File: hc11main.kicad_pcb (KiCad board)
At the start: 2 copper layers, 100 x 71 mm, 76 parts, among them J1 SPI, J2 CONN_I2C, J3 CONN_PWR, J4 CONN_LED, J5 CONN_UART, P1 CONN_2X20, T1 BS170/2N7000 (SOT23), T2 BS170/2N7000 (SOT23), U1 74LS138, U10 74LS10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

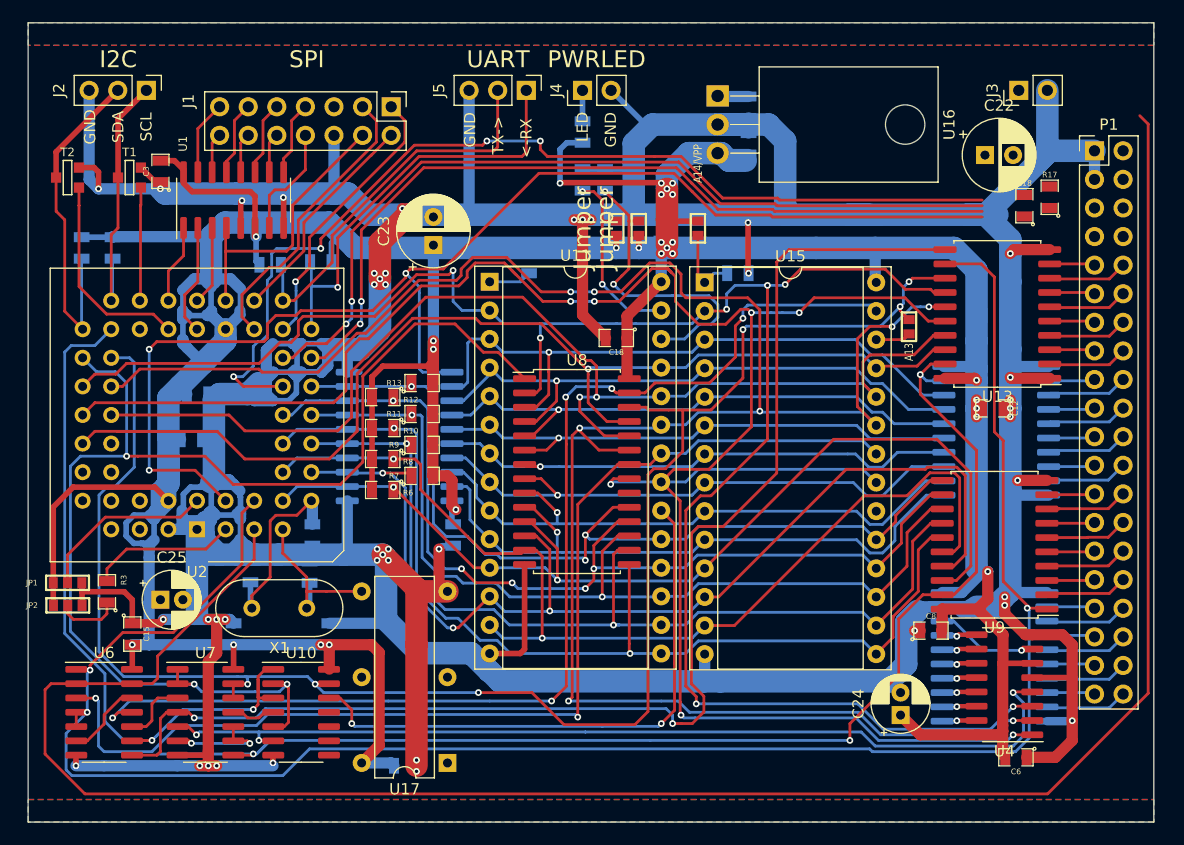
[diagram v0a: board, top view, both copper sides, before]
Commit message: finish routing everything, optimize routing, fix 2 missing CS traces
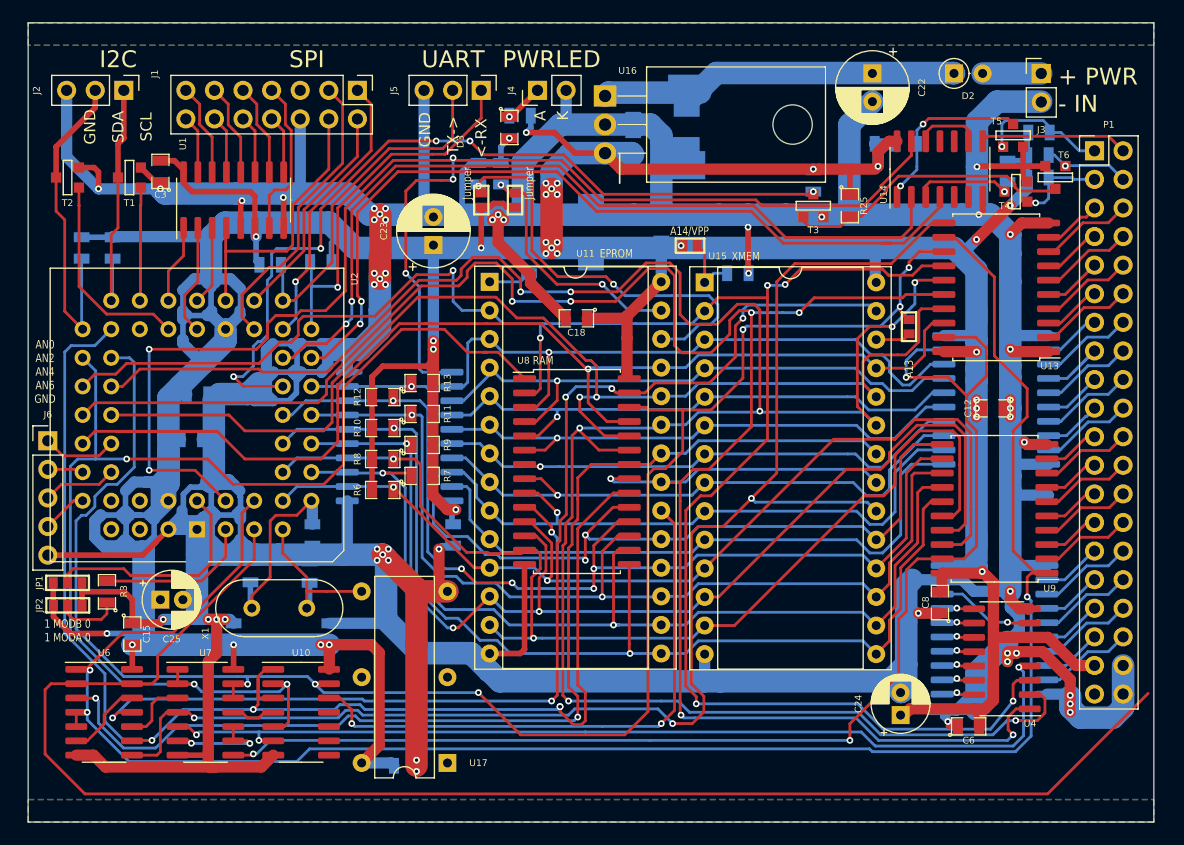
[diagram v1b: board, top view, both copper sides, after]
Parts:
- removed R17, R18: 100k, hc11:0805_m2012
- added C13: 100n, hc11:0805_m2012, B.Cu at (89.2, 25.8)
- added D1: SMBJ15A, hc11:D_SMB, B.Cu at (73.5, 24.2)
- added D2: Schottky, Diode_THT:D_DO-35_SOD27_P2.54mm_Vertical_AnodeUp, F.Cu at (97.2, 19.5)
- added D3: LED, hc11:0805_m2012, F.Cu at (57.8, 24.3)
- added D4: SMCJ15A, hc11:D_SMC, B.Cu at (73.5, 24.2)
- added D5: SMBJ5A, hc11:D_SMB, B.Cu at (65.0, 33.6)
- added J6: Conn_01x05, hc11:PinHeader_1x05_P2.54mm_Vertical, F.Cu at (16.8, 52.1)
- added R22: 10k, hc11:0805_m2012, B.Cu at (84.8, 29.0)
- added R23: 10k, hc11:0805_m2012, B.Cu at (102.0, 28.2)
- added R24: 10k, hc11:0805_m2012, B.Cu at (93.0, 25.8)
- added R25: 10k, hc11:0805_m2012, F.Cu at (88.0, 31.2)
- added R26: 10k, hc11:0805_m2012, B.Cu at (104.7, 28.8)
- added R27: 10k, hc11:0805_m2012, B.Cu at (104.8, 24.8)
- added R28: 10k, hc11:0805_m2012, B.Cu at (104.7, 26.8)
- added T3: BS170, hc11:SOT23GDS, F.Cu at (84.8, 31.2)
- added T4: BS170, hc11:SOT23GDS, F.Cu at (102.8, 30.0)
- added T5: BS170, hc11:SOT23GDS, F.Cu at (102.5, 25.0)
- added T6: BS170, hc11:SOT23GDS, F.Cu at (106.2, 28.7)
- added U14: 74HCT04, hc11:SOIC-14_3.9x8.7mm_P1.27mm, F.Cu at (96.0, 28.0)
- moved JP6 14.2 mm to (55.2, 30.8)
- moved C22 12.4 mm to (90.0, 19.5), turned to 270 degrees
- moved R15 11.3 mm to (55.0, 28.4)
- moved C19 10.3 mm to (68.8, 22.4)
- moved C20 10.2 mm to (68.8, 25.8)
- moved U16 10.0 mm to (66.2, 21.5)
- moved JP5 9.34 mm to (58.2, 30.8)
- moved R16 7.27 mm to (57.0, 28.4)
- moved R20 5.73 mm to (58.7, 23.2), turned to 180 degrees
- moved C6 5.02 mm to (98.5, 77.5), turned to 0 degrees
- moved J4 4.00 mm to (60.2, 21.0)
- moved J5 4.00 mm to (55.2, 21.0)
- moved C18 3.96 mm to (63.7, 41.2)
- moved J1 3.34 mm to (44.2, 21.0)
- moved U9 3.19 mm to (100.8, 58.2)
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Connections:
- net Net-(JP5-Pad1) renamed /EP_A14
- net Net-(JP6-Pad1) renamed /EP_A13
- J1 pad 10: /SPICS5 -> /SPICS4
- J1 pad 11: /SPICS2 -> /SPICS3
- J1 pad 12: /SPICS3 -> /SPICS2
- J1 pad 13: /SPICS0 -> /SPICS1
- J1 pad 14: /SPICS1 -> /SPICS0
- J1 pad 7: /SPICS6 -> /SPICS7
- J1 pad 8: /SPICS7 -> /SPICS6
- J1 pad 9: /SPICS4 -> /SPICS5
- P1 pad 1: GND -> /b~IRQ
- P1 pad 10: /bR~W -> /bA10
- P1 pad 11: /bA13 -> /bA9
- P1 pad 12: /bA12 -> /bA8
- P1 pad 13: /bA11 -> /bA7
- P1 pad 14: /bA10 -> /bA6
- P1 pad 15: /bA9 -> /bA5
- P1 pad 16: /bA8 -> /bA4
- P1 pad 17: /bA7 -> /bA3
- P1 pad 18: /bA6 -> /bA2
- P1 pad 19: /bA5 -> /bA1
- P1 pad 2: /bE -> /bAS
- P1 pad 20: /bA4 -> /bA0
- P1 pad 21: /bA3 -> /bD7
- P1 pad 22: /bA2 -> /bD6
- P1 pad 23: /bA1 -> /bD5
- P1 pad 24: /bA0 -> /bD4
- P1 pad 25: /bD7 -> /bD3
- P1 pad 26: /bD6 -> /bD2
- P1 pad 27: /bD5 -> /bD1
- P1 pad 28: /bD4 -> /bD0
- P1 pad 29: /bD3 -> /bS7
- P1 pad 3: GND -> /b~XIRQ
- P1 pad 30: /bD2 -> /bS6
- P1 pad 31: /bD1 -> /bS5
- P1 pad 32: /bD0 -> /bS4
- P1 pad 33: /bS7 -> /bS3
- P1 pad 34: /bS6 -> /bS2
- P1 pad 35: /bS5 -> /bS1
- P1 pad 36: /bS4 -> /bS0
- P1 pad 37: /bS3 -> VCC
- P1 pad 38: /bS2 -> GND
- P1 pad 39: /bS1 -> /bE
- P1 pad 4: VCC -> /b~RST
- P1 pad 40: /bS0 -> GND
- P1 pad 5: /bXIRQ -> /b~CSXRAM
- P1 pad 6: VCC -> /bR~W
- P1 pad 7: /bIRQ -> /bA13
- P1 pad 8: /bRST -> /bA12
- P1 pad 9: /b~CSXRAM -> /bA11
- U15 pad 20: /CSXRAM -> /~CSXRAM
- U8 pad 20: /~CSRAM -> /A15
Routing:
- net VCC: track 437.5 -> 519.5 mm, vias 26 -> 31
- net GND: track 632.6 -> 695.1 mm, vias 46 -> 50
- net /A15: track 64.8 -> 119.0 mm, vias 2 -> 4
- net /E: track 187.7 -> 136.1 mm
- net /VIN: track 2.77 -> 34.7 mm
- net /CPURST: track 0.00 -> 25.5 mm
- net /AS: track 113.8 -> 129.2 mm, vias 3 -> 5
- net /IRQ: track 0.00 -> 14.9 mm, vias 0 -> 2
- net /~CPURST: track 88.1 -> 74.1 mm, vias 4 -> 5
- net /bAS: track 0.00 -> 13.2 mm
- net /b~IRQ: track 0.00 -> 11.9 mm, vias 0 -> 1
- net /~CSXRAM: track 116.3 -> 127.6 mm, vias 2 -> 3
- net /EP_A13: track 27.6 -> 38.2 mm
- net /A11: track 194.9 -> 204.7 mm
- net /XIRQ: track 0.00 -> 9.45 mm, vias 0 -> 1
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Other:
- board text added: "+ PWR - IN"
- board text added: "1 MODB 0 1 MODA 0"
- board text added: "A"
- board text added: "AN0 AN2 AN4 AN6 GND"
- board text added: "EPROM"
- board text added: "K"
- board text added: "RAM"
- board text added: "XMEM"
- board text removed: "LED"

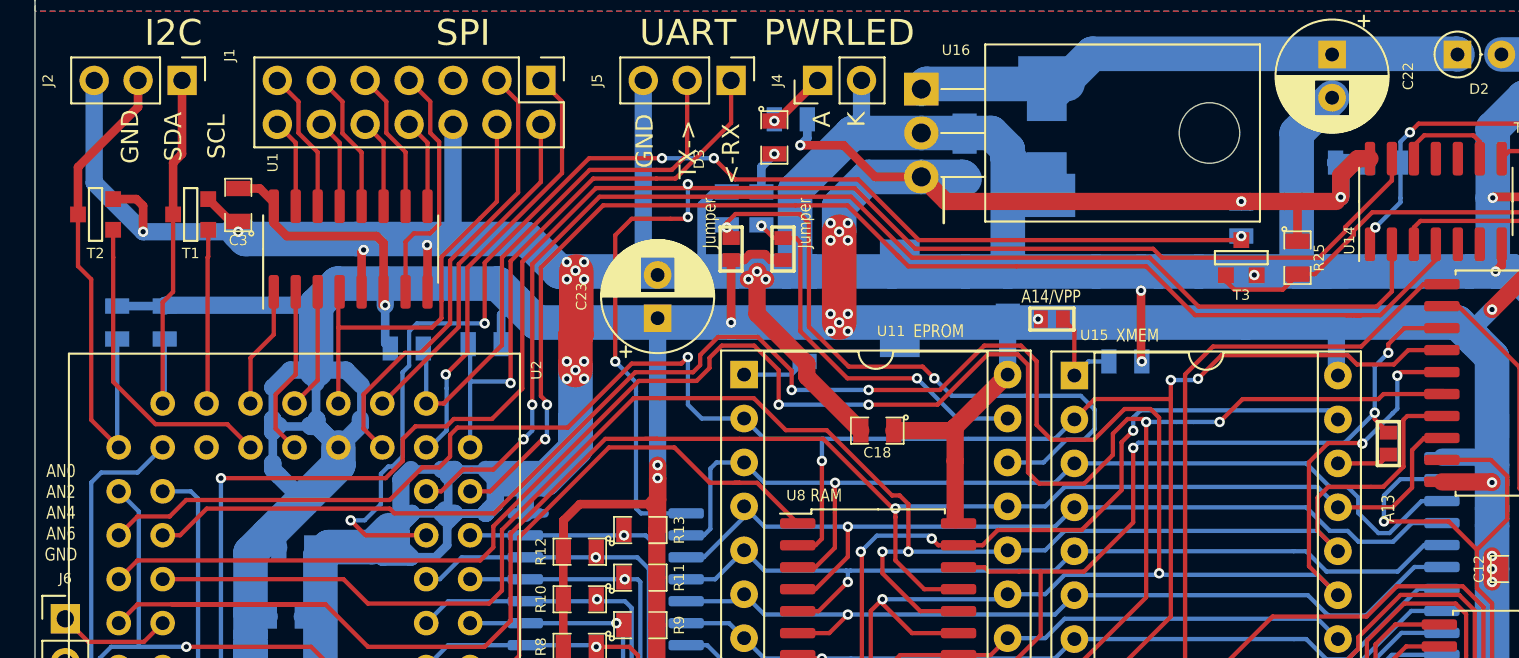
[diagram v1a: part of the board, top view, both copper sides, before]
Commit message: update some labels
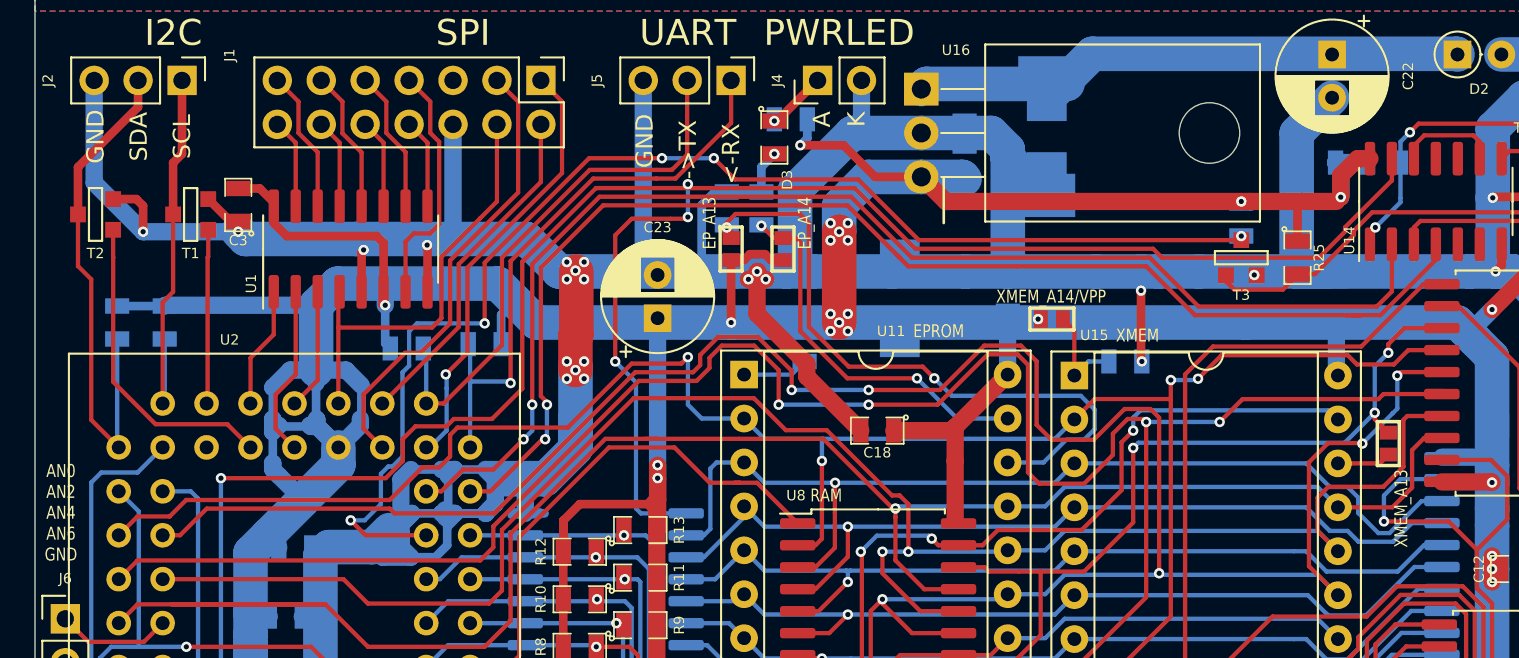
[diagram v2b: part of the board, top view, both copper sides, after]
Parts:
- JP3: value A13 -> XMEM_A13
- JP5: value Jumper -> EP_A14
- JP6: value Jumper -> EP_A13
- JP7: value A14/VPP -> XMEM_A14/VPP
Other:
- board text added: "->TX"
- board text removed: "TX->"
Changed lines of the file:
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@@
     (at 57.75 24.2975 270)
     (attr smd)
-    (fp_text reference D3 (at 1.25 4.35 90) (layer F.SilkS)
+    (fp_text reference D3 (at 2.4525 -0.75 90) (layer F.SilkS)
       (effects (font (size 0.6 0.6) (thickness 0.15)))
     )
@@
     (descr "PLCC, 52 pins, through hole")
     (tags "plcc leaded")
-    (fp_text reference U2 (at -14 22.25 90) (layer F.SilkS)
+    (fp_text reference U2 (at 3.75 24 180) (layer F.SilkS)
       (effects (font (size 0.6 0.6) (thickness 0.15)))
     )
@@
     (descr "CP, Radial series, Radial, pin pitch=2.50mm, , diameter=6.3mm, Electrolytic Capacitor")
     (tags "CP Radial series Radial pin pitch 2.50mm  diameter 6.3mm Electrolytic Capacitor")
-    (fp_text reference C23 (at 1.25 -4.4 90) (layer F.SilkS)
+    (fp_text reference C23 (at 5.25 0 180) (layer F.SilkS)
       (effects (font (size 0.6 0.6) (thickness 0.15)))
     )
@@
       (effects (font (size 1.524 1.524) (thickness 0.3048)))
     )
-    (fp_text value A14/VPP (at 0.05 1.3) (layer F.SilkS)
+    (fp_text value XMEM_A14/VPP (at 0.05 1.3) (layer F.SilkS)
       (effects (font (size 0.75 0.6) (thickness 0.15)))
     )
@@
       (effects (font (size 1.524 1.524) (thickness 0.3048)))
     )
-    (fp_text value A13 (at -3.75 0 90) (layer F.SilkS)
+    (fp_text value XMEM_A13 (at -3.75 0.75 90) (layer F.SilkS)
       (effects (font (size 0.75 0.6) (thickness 0.125)))
     )
@@
       (effects (font (size 1.524 1.524) (thickness 0.3048)))
     )
-    (fp_text value Jumper (at -1.5 1.25 90) (layer F.SilkS)
+    (fp_text value EP_A13 (at -1.5 1.25 90) (layer F.SilkS)
       (effects (font (size 0.75 0.6) (thickness 0.15)))
     )
@@
       (effects (font (size 1.524 1.524) (thickness 0.3048)))
     )
-    (fp_text value Jumper (at -1.5 -1.25 90) (layer F.SilkS)
+    (fp_text value EP_A14 (at -1.5 -1.25 90) (layer F.SilkS)
       (effects (font (size 0.75 0.6) (thickness 0.15)))
     )
@@
     (tags "SOIC SO")
     (attr smd)
-    (fp_text reference U1 (at 5 -4.5 90) (layer F.SilkS)
+    (fp_text reference U1 (at -2 -5.75 90) (layer F.SilkS)
       (effects (font (size 0.6 0.6) (thickness 0.15)))
     )
@@
     (effects (font (size 1 1) (thickness 0.25)))
   )
-  (gr_text TX-> (at 52.75 25 90) (layer F.SilkS)
+  (gr_text ->TX (at 52.75 25 90) (layer F.SilkS)
     (effects (font (size 1 1) (thickness 0.25)))
   )
@@
     (effects (font (size 1.5 1.5) (thickness 0.3)))
   )
-  (gr_text GND (at 20.5 24.25 90) (layer F.SilkS)
+  (gr_text GND (at 18.5 24.25 90) (layer F.SilkS)
     (effects (font (size 1 1) (thickness 0.25)))
   )
-  (gr_text SDA (at 23 24.25 90) (layer F.SilkS)
+  (gr_text SDA (at 21 24.25 90) (layer F.SilkS)
     (effects (font (size 1 1) (thickness 0.25)))
   )
-  (gr_text SCL (at 25.5 24.25 90) (layer F.SilkS)
+  (gr_text SCL (at 23.5 24.25 90) (layer F.SilkS)
     (effects (font (size 1 1) (thickness 0.25)))
   )

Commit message: board optimizations
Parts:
- added C26: 100n, hc11:0805_m2012, F.Cu at (110.2, 82.2)
- added JP10: SIRQ, hc11:SMDPADS_2, F.Cu at (96.8, 23.2)
- added JP4: XMEM_WR, hc11:SMDPADS_2, B.Cu at (83.8, 40.2)
- added JP8: XMEM_WRL, hc11:SMDPADS_2, B.Cu at (87.2, 40.2)
- added JP9: XMEM_WRH, hc11:SMDPADS_2, B.Cu at (85.5, 40.2)
- added T7: BS250 (SOT23), hc11:SOT23GDS, F.Cu at (107.6, 79.5)
- added T8: BS170 (SOT23), hc11:SOT23GDS, F.Cu at (111.1, 79.5)
- C13: moved to F.Cu
- moved R24 2.14 mm to (92.2, 27.8)
- moved C8 1.41 mm to (95.0, 65.5), turned to 0 degrees
- moved R27 1.00 mm to (104.8, 25.8)
- moved R26 1.00 mm to (104.7, 29.8)
- moved R28 1.00 mm to (104.7, 27.8)
- moved T5 0.75 mm to (102.5, 25.8), turned to 270 degrees
- moved C24 0.71 mm to (92.0, 77.0)
- moved J6 0.50 mm to (16.2, 52.1)
- moved C13 0.39 mm to (89.5, 26.0)
- moved JP3 0.25 mm to (93.0, 42.0)
- moved R1 0.25 mm to (41.0, 36.5)
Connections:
- J1 pad 5: Net-(J1-Pad5) -> /SIRQ
- U10 pad 10: (no net) -> /E
- U10 pad 11: (no net) -> /E
- U10 pad 8: (no net) -> /~E
- U10 pad 9: (no net) -> /E
- U15 pad 27: /~WR -> Net-(JP4-Pad1)
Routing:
- net GND: track 695.1 -> 1012.3 mm, vias 50 -> 156
- net /E: track 136.1 -> 64.0 mm
- net /~E: track 0.00 -> 70.5 mm, vias 0 -> 2
- net /SIRQ: track 0.00 -> 65.3 mm
- net VCC: track 519.5 -> 553.5 mm, vias 31 -> 34
- net /R~W: track 172.5 -> 192.9 mm
- net /~CSXRAM: track 127.6 -> 140.3 mm
- net /~WR: track 103.0 -> 92.4 mm
- net /~CSEXT: track 113.8 -> 104.5 mm
- net /b~IRQ: track 11.9 -> 20.5 mm
- net /bE: track 0.00 -> 7.34 mm
- net Net-(JP4-Pad1): track 0.00 -> 6.70 mm
- net /A11: track 204.7 -> 209.1 mm
- net /IRQ: track 14.9 -> 11.4 mm
- net /A15: track 119.0 -> 115.4 mm, vias 4 -> 3
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- added copper zone on B.Cu, net GND
- added copper zone on F.Cu, net GND
- removed copper zone on B.Cu, net (none)
- removed copper zone on F.Cu, net (none)
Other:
- board text added: "(c) 2020 by Sebastien F4GRX - rev 1.0"
- board text added: "SYS11 mainboard"
